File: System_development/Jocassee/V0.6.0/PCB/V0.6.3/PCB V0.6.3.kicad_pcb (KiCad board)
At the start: 2 copper layers, 33 x 122.5 mm, 32 parts, among them J1 TDS PRB, J2 Temp, J3 BAT, J4 TRBDT, J5 CHRG, J6 Conn_Coaxial_Small, P1 SD card socket, Q1 2N2222A, U1 NRF24L01+PA+LNA, U2 ProMicro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

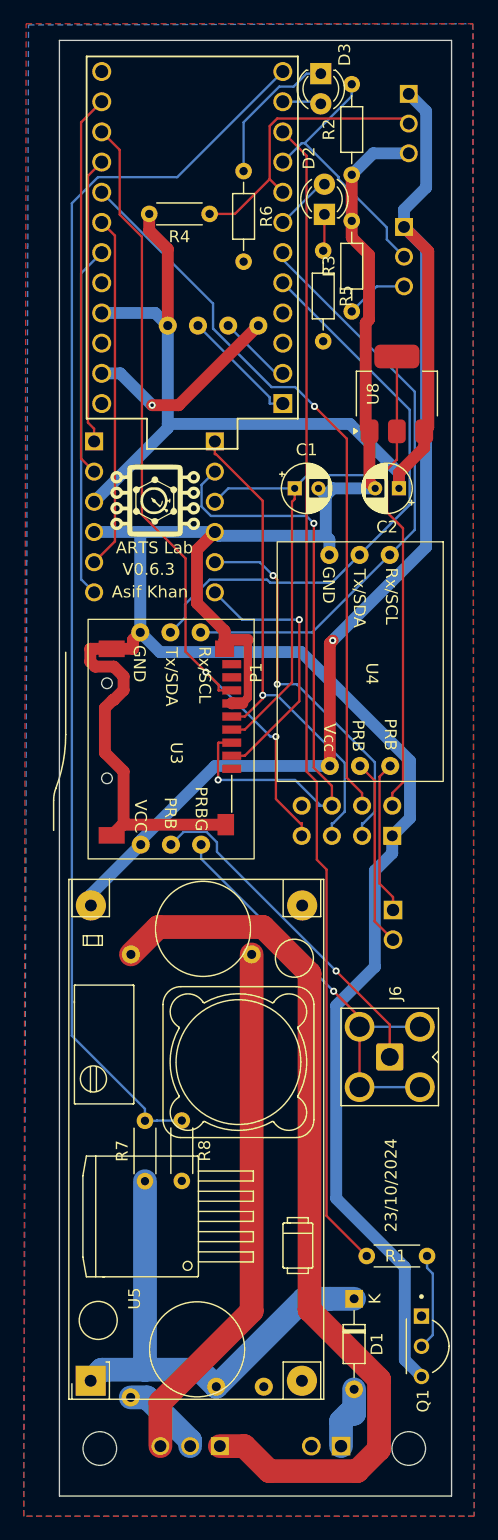
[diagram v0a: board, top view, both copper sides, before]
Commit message: Group members name added in PCB
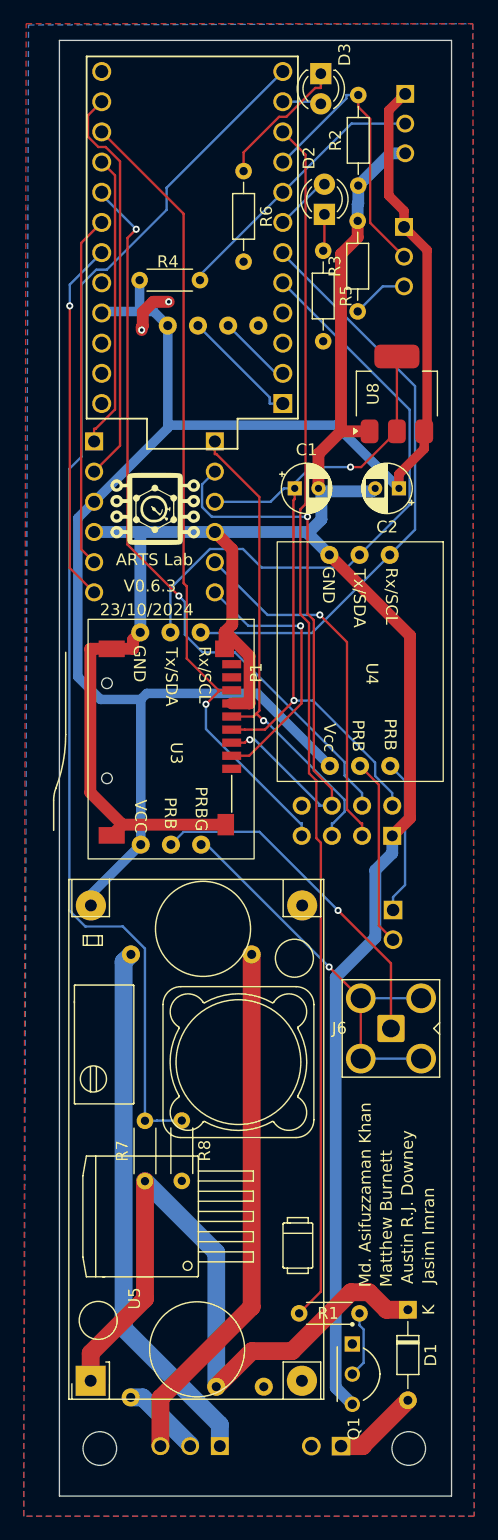
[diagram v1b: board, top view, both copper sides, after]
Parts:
- moved R1 7.46 mm to (99.8, 171.6)
- moved Q1 6.27 mm to (106.6, 176.7)
- moved R4 5.63 mm to (91.4, 84.7)
- moved D1 4.62 mm to (108.9, 171.3)
- moved J6 2.40 mm to (107.5, 147.7)
- moved R2 1.06 mm to (104.8, 76.7)
- moved ARTS Lab 0.70 mm to (87.7, 104.0)
- moved R3 0.50 mm to (104.7, 87.3)
- moved J2 0.30 mm to (109.2, 71.5)
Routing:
- net BAT+: track 75.1 -> 45.0 mm
- net 5V: track 167.6 -> 143.0 mm, vias 1 -> 0
- net CHRG rectified: track 42.1 -> 58.5 mm
- net 3.3V: track 77.6 -> 61.9 mm, vias 1 -> 2
- net GND: track 17.1 -> 4.08 mm, vias 1 -> 2
- net V GND: track 209.2 -> 200.0 mm
- net P_EN: track 97.5 -> 101.9 mm
- net Net-(P1-CMD/MOSI): track 52.6 -> 48.7 mm
- net SDA: track 48.6 -> 51.1 mm
- net Net-(Q1-Pad2): track 8.19 -> 5.65 mm
- net Net-(J6-Ext): track 36.1 -> 34.0 mm
- net Net-(U2-D7): track 22.1 -> 24.1 mm
- net CHRG IN: track 5.51 -> 7.26 mm
- net Net-(P1-CLK/SCK): track 42.5 -> 40.8 mm
- net MOSI: track 32.3 -> 34.0 mm
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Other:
- board text added: "Austin R.J. Downey"
- board text added: "Jasim Imran"
- board text added: "Matthew Burnett"
- board text added: "Md. Asifuzzaman Khan"
- board text removed: "Asif Khan"
